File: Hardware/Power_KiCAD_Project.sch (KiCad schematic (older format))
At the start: 6 parts, among them J1 Barrel_Jack_MountingPin, J2 XT60 Cell 5, J3 XT60 Cell 4, J4 XT60 Cell 3, J5 XT60 Cell 2, J6 XT60 Cell 1

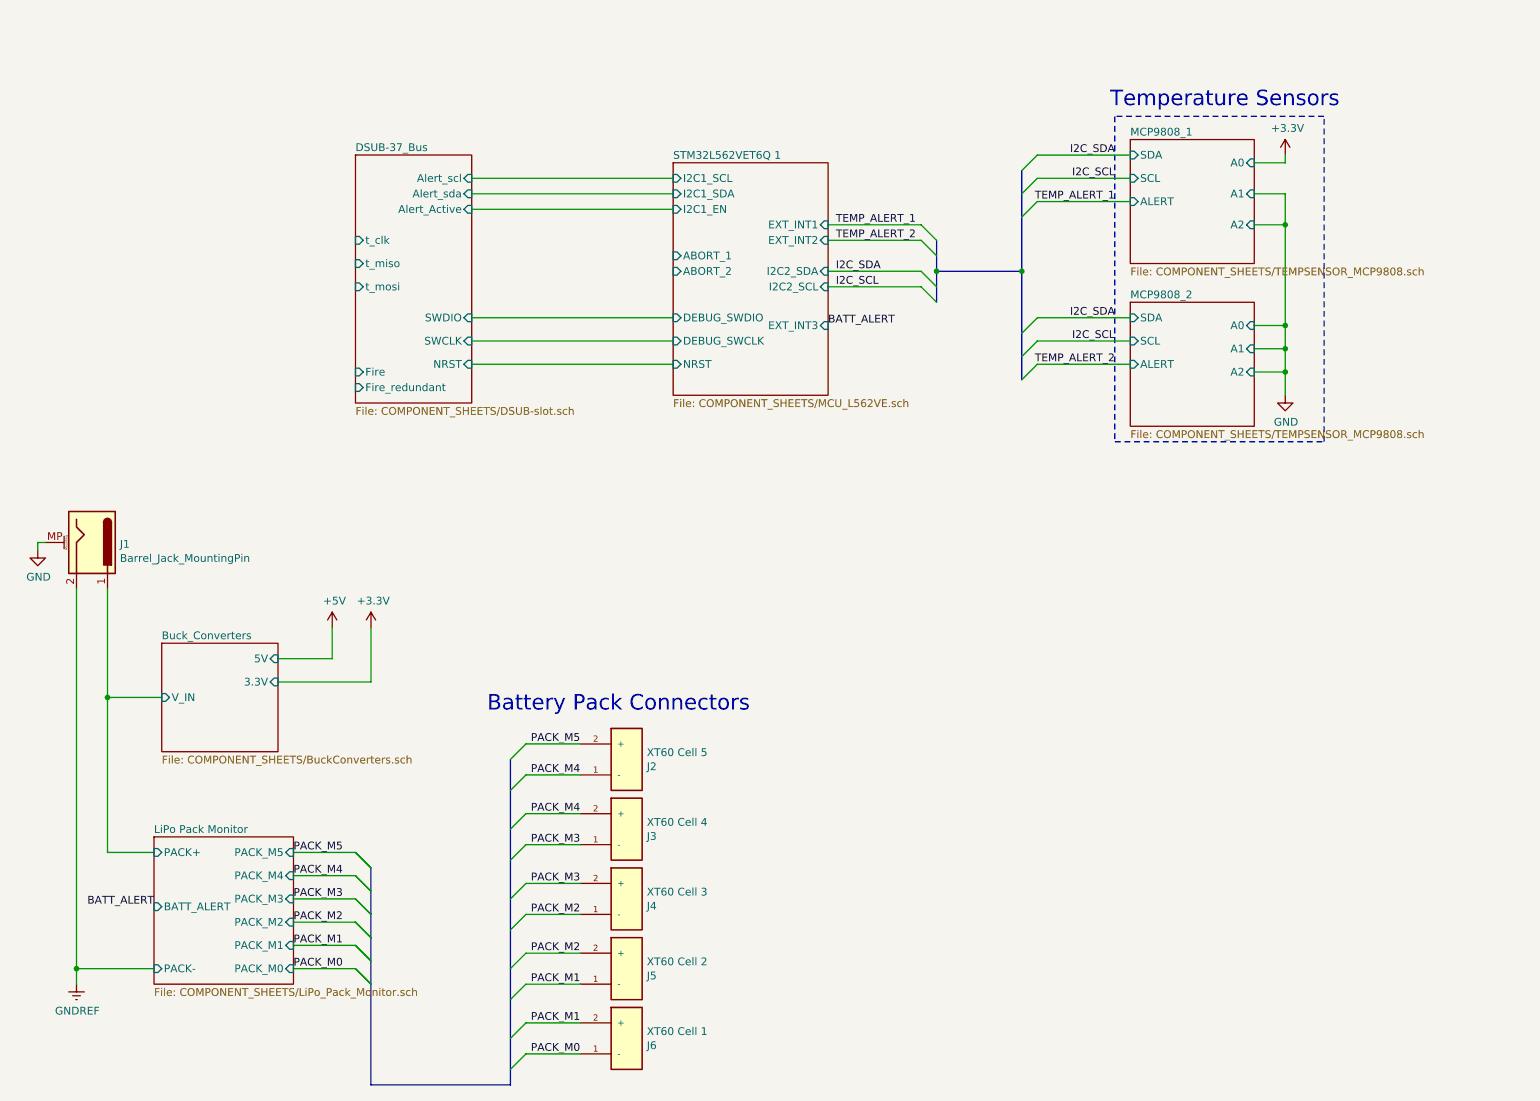
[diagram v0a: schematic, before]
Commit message: Added I2C lines to lipo monitor schematic page
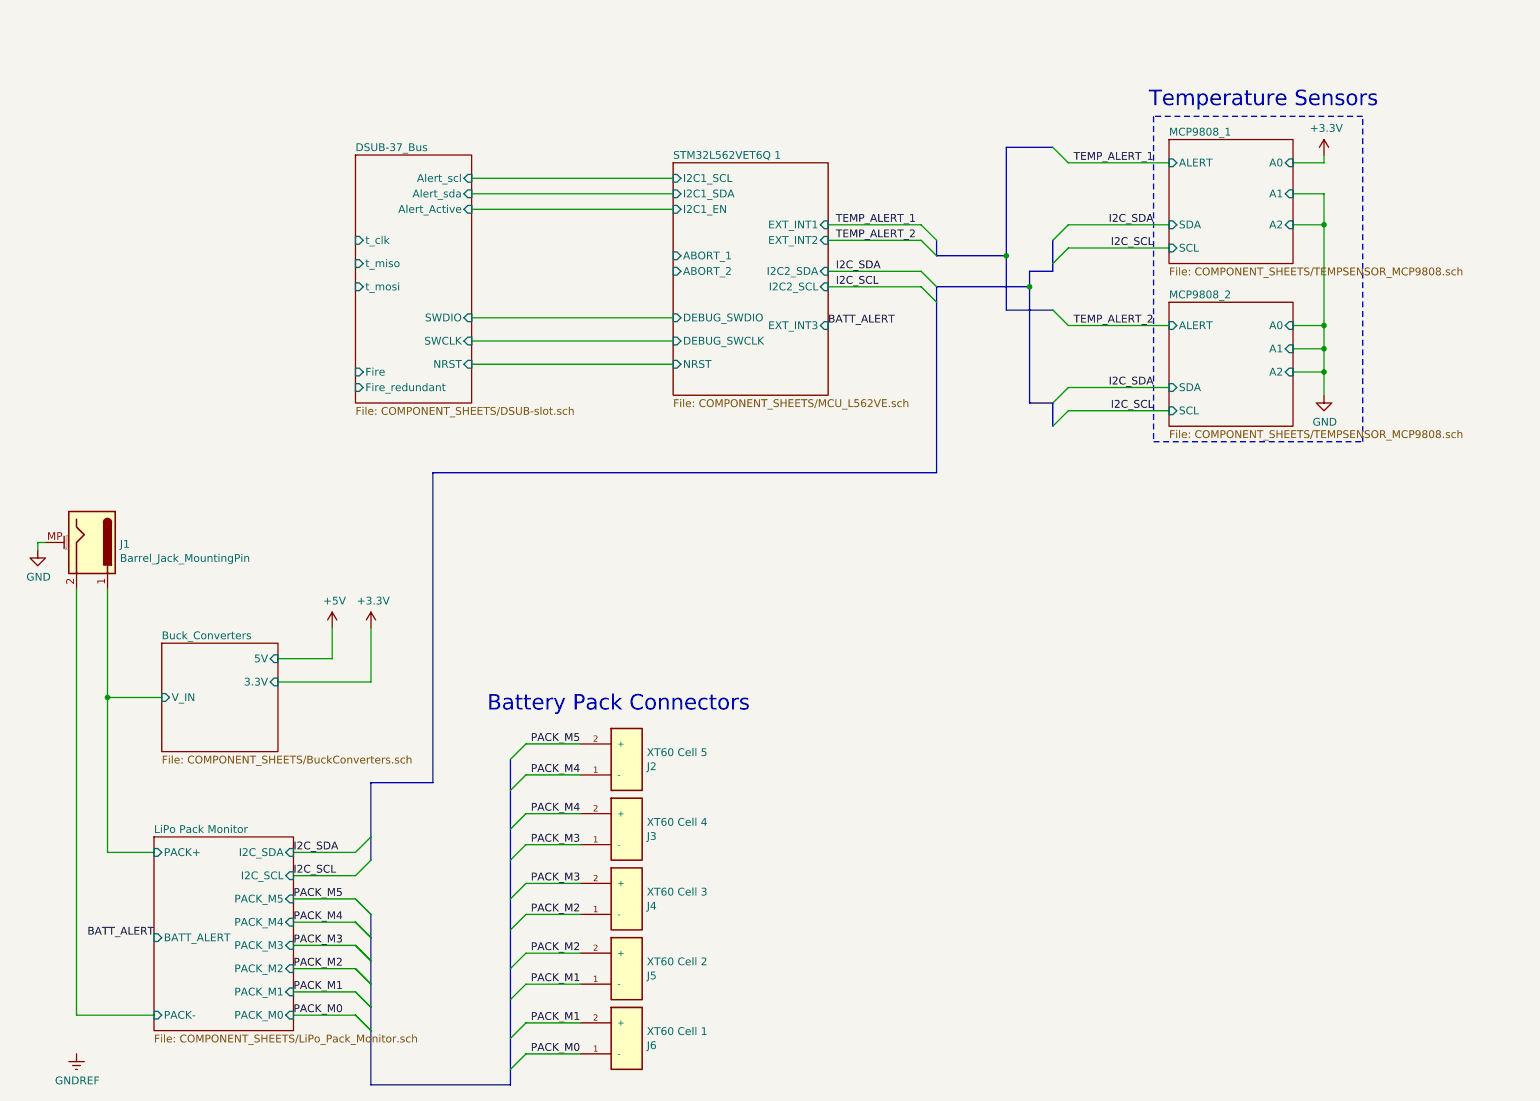
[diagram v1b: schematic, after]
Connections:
- net GNDREF: no longer J1.2
- new net LiPo Pack Monitor/PACK-: J1.2
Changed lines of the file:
@@
 L power:+3.3V #PWR05
 U 1 1 61B3C742
-P 9000 1500
-F 0 "#PWR05" H 9000 1350 50  0001 C CNN
-F 1 "+3.3V" H 9015 1673 50  0000 C CNN
-F 2 "" H 9000 1500 50  0001 C CNN
-F 3 "" H 9000 1500 50  0001 C CNN
-	1    9000 1500
+P 9250 1500
+F 0 "#PWR05" H 9250 1350 50  0001 C CNN
+F 1 "+3.3V" H 9265 1673 50  0000 C CNN
+F 2 "" H 9250 1500 50  0001 C CNN
+F 3 "" H 9250 1500 50  0001 C CNN
+	1    9250 1500
 	1    0    0    -1
 $EndComp
-Text Notes 9350 1200 2    100  ~ 0
+Text Notes 9600 1200 2    100  ~ 0
 Temperature Sensors
 $Sheet
-S 8000 2450 800  800
+S 8250 2450 800  800
 U 61B35621
 F0 "MCP9808_2" 50
 F1 "COMPONENT_SHEETS/TEMPSENSOR_MCP9808.sch" 50
-F2 "SDA" I L 8000 2550 50
-F3 "SCL" I L 8000 2700 50
-F4 "A0" I R 8800 2600 50
-F5 "A1" I R 8800 2750 50
-F6 "A2" I R 8800 2900 50
-F7 "ALERT" I L 8000 2850 50
+F2 "SDA" I L 8250 3000 50
+F3 "SCL" I L 8250 3150 50
+F4 "A0" I R 9050 2600 50
+F5 "A1" I R 9050 2750 50
+F6 "A2" I R 9050 2900 50
+F7 "ALERT" I L 8250 2600 50
 $EndSheet
 Entry Wire Line
@@
 I2C_SCL
 Wire Wire Line
-	9000 2900 8800 2900
-Wire Wire Line
-	9000 2900 9000 2750
-Wire Wire Line
-	9000 2750 8800 2750
-Wire Wire Line
-	9000 2750 9000 2600
-Wire Wire Line
-	9000 2600 8800 2600
-Connection ~ 9000 2750
-Wire Wire Line
-	8800 1950 9000 1950
-Connection ~ 9000 2600
-Wire Wire Line
-	8800 1750 9000 1750
-Wire Wire Line
-	9000 1750 9000 1950
-Connection ~ 9000 1950
-Wire Wire Line
-	8800 1550 9000 1550
-Wire Wire Line
-	9000 1550 9000 1500
+	9250 2900 9050 2900
+Wire Wire Line
+	9250 2900 9250 2750
+Wire Wire Line
+	9250 2750 9050 2750
+Wire Wire Line
+	9250 2750 9250 2600
+Wire Wire Line
+	9250 2600 9050 2600
+Connection ~ 9250 2750
+Wire Wire Line
+	9050 1950 9250 1950
+Connection ~ 9250 2600
+Wire Wire Line
+	9050 1750 9250 1750
+Wire Wire Line
+	9250 1750 9250 1950
+Connection ~ 9250 1950
+Wire Wire Line
+	9050 1550 9250 1550
+Wire Wire Line
+	9250 1550 9250 1500
 Wire Notes Line
-	9250 1250 7900 1250
+	9500 1250 8150 1250
 Entry Wire Line
 	6750 2050 6650 1950
@@
 Text Label 6100 2050 0    50   ~ 0
 TEMP_ALERT_2
-Text Label 7900 1800 2    50   ~ 0
+Text Label 8150 1550 2    50   ~ 0
 TEMP_ALERT_1
-Text Label 7900 1500 2    50   ~ 0
+Text Label 8150 1950 2    50   ~ 0
 I2C_SDA
-Text Label 7900 1650 2    50   ~ 0
+Text Label 8150 2100 2    50   ~ 0
 I2C_SCL
-Text Label 7900 2700 2    50   ~ 0
+Text Label 8150 3150 2    50   ~ 0
 I2C_SCL
-Text Label 7900 2550 2    50   ~ 0
+Text Label 8150 3000 2    50   ~ 0
 I2C_SDA
-Text Label 7900 2850 2    50   ~ 0
+Text Label 8150 2600 2    50   ~ 0
 TEMP_ALERT_2
 Entry Wire Line
-	3100 6100 3000 6000
-Entry Wire Line
-	3100 6250 3000 6150
-Entry Wire Line
 	3100 6400 3000 6300
 Entry Wire Line
@@
 	3100 6850 3000 6750
 Entry Wire Line
-	3100 6100 3000 6000
+	3100 7000 3000 6900
+Entry Wire Line
+	3100 7150 3000 7050
+Entry Wire Line
+	3100 6400 3000 6300
+Entry Wire Line
+	3100 7150 3000 7050
+Wire Wire Line
+	3000 7050 2600 7050
+Wire Wire Line
+	3000 6900 2600 6900
+Wire Wire Line
+	3000 6750 2600 6750
+Wire Wire Line
+	2600 6600 3000 6600
+Wire Wire Line
+	3000 6450 2600 6450
+Wire Wire Line
+	2600 6300 3000 6300
+Text Label 2600 6300 0    50   ~ 0
+PACK_M5
+Text Label 2600 6450 0    50   ~ 0
+PACK_M4
+Text Label 2600 6600 0    50   ~ 0
+PACK_M3
+Text Label 2600 6750 0    50   ~ 0
+PACK_M2
+Text Label 2600 6900 0    50   ~ 0
+PACK_M1
+Text Label 2600 7050 0    50   ~ 0
+PACK_M0
+Entry Wire Line
+	3100 7000 3000 6900
 Entry Wire Line
 	3100 6850 3000 6750
-Wire Wire Line
-	3000 6750 2600 6750
-Wire Wire Line
-	3000 6600 2600 6600
-Wire Wire Line
-	3000 6450 2600 6450
-Wire Wire Line
-	2600 6300 3000 6300
-Wire Wire Line
-	3000 6150 2600 6150
-Wire Wire Line
-	2600 6000 3000 6000
-Text Label 2600 6000 0    50   ~ 0
-PACK_M5
-Text Label 2600 6150 0    50   ~ 0
-PACK_M4
-Text Label 2600 6300 0    50   ~ 0
-PACK_M3
-Text Label 2600 6450 0    50   ~ 0
-PACK_M2
-Text Label 2600 6600 0    50   ~ 0
-PACK_M1
-Text Label 2600 6750 0    50   ~ 0
-PACK_M0
 Entry Wire Line
 	3100 6700 3000 6600
 Entry Wire Line
 	3100 6550 3000 6450
-Entry Wire Line
-	3100 6400 3000 6300
-Entry Wire Line
-	3100 6250 3000 6150
-Wire Wire Line
-	7400 2550 8000 2550
-Wire Wire Line
-	8000 2700 7400 2700
-Wire Wire Line
-	7400 2850 8000 2850
-Wire Wire Line
-	7400 1800 8000 1800
-Wire Wire Line
-	7400 1650 8000 1650
-Wire Wire Line
-	7400 1500 8000 1500
-Entry Wire Line
-	7300 2650 7400 2550
-Entry Wire Line
-	7300 2800 7400 2700
-Entry Wire Line
-	7300 2950 7400 2850
-Entry Wire Line
-	7300 1900 7400 1800
-Entry Wire Line
-	7300 1750 7400 1650
-Entry Wire Line
-	7300 1600 7400 1500
 Connection ~ 1400 5000
 Wire Wire Line
@@
 $EndComp
 $Sheet
-S 8000 1400 800  800
+S 8250 1400 800  800
 U 61B1B3BC
 F0 "MCP9808_1" 50
 F1 "COMPONENT_SHEETS/TEMPSENSOR_MCP9808.sch" 50
-F2 "SDA" I L 8000 1500 50
-F3 "SCL" I L 8000 1650 50
-F4 "A0" I R 8800 1550 50
-F5 "A1" I R 8800 1750 50
-F6 "A2" I R 8800 1950 50
-F7 "ALERT" I L 8000 1800 50
+F2 "SDA" I L 8250 1950 50
+F3 "SCL" I L 8250 2100 50
+F4 "A0" I R 9050 1550 50
+F5 "A1" I R 9050 1750 50
+F6 "A2" I R 9050 1950 50
+F7 "ALERT" I L 8250 1550 50
 $EndSheet
 $Sheet
@@
 $EndSheet
 $Sheet
-S 1700 5900 900  950
+S 1700 5900 900  1250
 U 615ED460
 F0 "LiPo Pack Monitor" 50
 F1 "COMPONENT_SHEETS/LiPo_Pack_Monitor.sch" 50
 F2 "PACK+" I L 1700 6000 50
-F3 "PACK_M5" I R 2600 6000 50
-F4 "PACK_M4" I R 2600 6150 50
-F5 "PACK_M3" I R 2600 6300 50
-F6 "PACK_M2" I R 2600 6450 50
-F7 "PACK_M1" I R 2600 6600 50
-F8 "PACK_M0" I R 2600 6750 50
-F9 "PACK-" I L 1700 6750 50
-F10 "BATT_ALERT" I L 1700 6350 50
+F3 "PACK_M5" I R 2600 6300 50
+F4 "PACK_M4" I R 2600 6450 50
+F5 "PACK_M3" I R 2600 6600 50
+F6 "PACK_M2" I R 2600 6750 50
+F7 "PACK_M1" I R 2600 6900 50
+F8 "PACK_M0" I R 2600 7050 50
+F9 "PACK-" I L 1700 7050 50
+F10 "BATT_ALERT" I L 1700 6550 50
+F11 "I2C_SCL" I R 2600 6150 50
+F12 "I2C_SDA" I R 2600 6000 50
 $EndSheet
 Wire Notes Line
-	7900 1250 7900 3350
+	8150 1250 8150 3350
 Wire Notes Line
-	9250 3350 9250 1250
+	9500 3350 9500 1250
 Wire Notes Line
-	7900 3350 9250 3350
+	8150 3350 9500 3350
 Wire Wire Line
 	2500 4750 2850 4750
@@
 L power:GNDREF #PWR02
 U 1 1 61C61481
-P 1200 6850
-F 0 "#PWR02" H 1200 6600 50  0001 C CNN
-F 1 "GNDREF" H 1205 6677 50  0000 C CNN
-F 2 "" H 1200 6850 50  0001 C CNN
-F 3 "" H 1200 6850 50  0001 C CNN
-	1    1200 6850
+P 1200 7300
+F 0 "#PWR02" H 1200 7050 50  0001 C CNN
+F 1 "GNDREF" H 1205 7127 50  0000 C CNN
+F 2 "" H 1200 7300 50  0001 C CNN
+F 3 "" H 1200 7300 50  0001 C CNN
+	1    1200 7300
 	1    0    0    -1
 $EndComp
@@
 Wire Wire Line
 	4450 7300 4100 7300
-Wire Wire Line
-	1200 4300 1200 6750
-Connection ~ 1200 6750
-Wire Wire Line
-	1200 6750 1200 6850
 $Sheet
 S 5050 1550 1000 1500
@@
 Text Label 6050 2600 0    50   ~ 0
 BATT_ALERT
-Text Label 1700 6350 2    50   ~ 0
+Text Label 1700 6550 2    50   ~ 0
 BATT_ALERT
 Wire Wire Line
 	1400 6000 1700 6000
-Wire Wire Line
-	1200 6750 1700 6750
 Text Notes 3850 5100 0    100  ~ 0
 Battery Pack Connectors
-Connection ~ 9000 2900
-Wire Wire Line
-	9000 3050 9000 2900
+Connection ~ 9250 2900
+Wire Wire Line
+	9250 3050 9250 2900
 $Comp
 L power:GND #PWR06
 U 1 1 61CCB2E2
-P 9000 3050
-F 0 "#PWR06" H 9000 2800 50  0001 C CNN
-F 1 "GND" H 9005 2877 50  0000 C CNN
-F 2 "" H 9000 3050 50  0001 C CNN
-F 3 "" H 9000 3050 50  0001 C CNN
-	1    9000 3050
+P 9250 3050
+F 0 "#PWR06" H 9250 2800 50  0001 C CNN
+F 1 "GND" H 9255 2877 50  0000 C CNN
+F 2 "" H 9250 3050 50  0001 C CNN
+F 3 "" H 9250 3050 50  0001 C CNN
+	1    9250 3050
 	1    0    0    -1
 $EndComp
 Wire Wire Line
-	9000 1950 9000 2600
+	9250 1950 9250 2600
 Wire Wire Line
 	1400 5000 1750 5000
@@
 Wire Wire Line
 	5050 2850 3750 2850
-Wire Bus Line
-	6750 2250 7300 2250
-Connection ~ 7300 2250
-Connection ~ 6750 2250
 $Comp
 L power:GND #PWR?
@@
 Wire Wire Line
 	3750 1850 5050 1850
-Wire Bus Line
-	6750 2050 6750 2250
-Wire Bus Line
-	6750 2250 6750 2450
-Wire Bus Line
-	7300 2250 7300 2950
-Wire Bus Line
-	7300 1600 7300 2250
-Wire Bus Line
-	3100 6100 3100 7500
+Wire Wire Line
+	1200 7050 1700 7050
+Wire Wire Line
+	1200 4300 1200 7050
+Wire Wire Line
+	2600 6150 3000 6150
+Wire Wire Line
+	2600 6000 3000 6000
+Text Label 2600 6150 0    50   ~ 0
+I2C_SCL
+Text Label 2600 6000 0    50   ~ 0
+I2C_SDA
+Entry Wire Line
+	3000 6150 3100 6050
+Entry Wire Line
+	3000 6000 3100 5900
+Wire Bus Line
+	3100 5550 3500 5550
+Wire Bus Line
+	3500 5550 3500 3550
+Wire Bus Line
+	3500 3550 6750 3550
+Wire Bus Line
+	6750 2050 6750 2150
+Wire Bus Line
+	6750 2150 7200 2150
+Entry Wire Line
+	7600 1950 7500 2050
+Entry Wire Line
+	7600 2100 7500 2200
+Entry Wire Line
+	7600 3000 7500 3100
+Entry Wire Line
+	7600 3150 7500 3250
+Entry Wire Line
+	7600 2600 7500 2500
+Entry Wire Line
+	7600 1550 7500 1450
+Wire Bus Line
+	7500 3250 7500 3100
+Wire Bus Line
+	7500 3100 7350 3100
+Wire Bus Line
+	7200 2150 7200 1450
+Wire Bus Line
+	7200 1450 7500 1450
+Wire Bus Line
+	7500 2500 7200 2500
+Wire Bus Line
+	6750 2350 7350 2350
+Wire Bus Line
+	7200 2500 7200 2150
+Connection ~ 7200 2150
+Wire Bus Line
+	7350 2350 7350 3100
+Wire Bus Line
+	7350 2350 7350 2250
+Wire Bus Line
+	7350 2250 7500 2250
+Connection ~ 7350 2350
+Wire Wire Line
+	7600 1950 8250 1950
+Wire Wire Line
+	7600 2100 8250 2100
+Wire Wire Line
+	7600 2600 8250 2600
+Wire Wire Line
+	7600 3000 8250 3000
+Wire Wire Line
+	7600 3150 8250 3150
+Wire Wire Line
+	7600 1550 8250 1550
+Wire Bus Line
+	3100 5550 3100 6050
+Wire Bus Line
+	6750 2350 6750 3550
+Wire Bus Line
+	7500 2050 7500 2250
+Wire Bus Line
+	3100 6400 3100 7500
 Wire Bus Line
 	4000 5400 4000 7500

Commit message: Moved external switch connector to pack+, added missing no connection flags
This change renders the current PCB layout defunct, next commits will be redesigns of the layout.
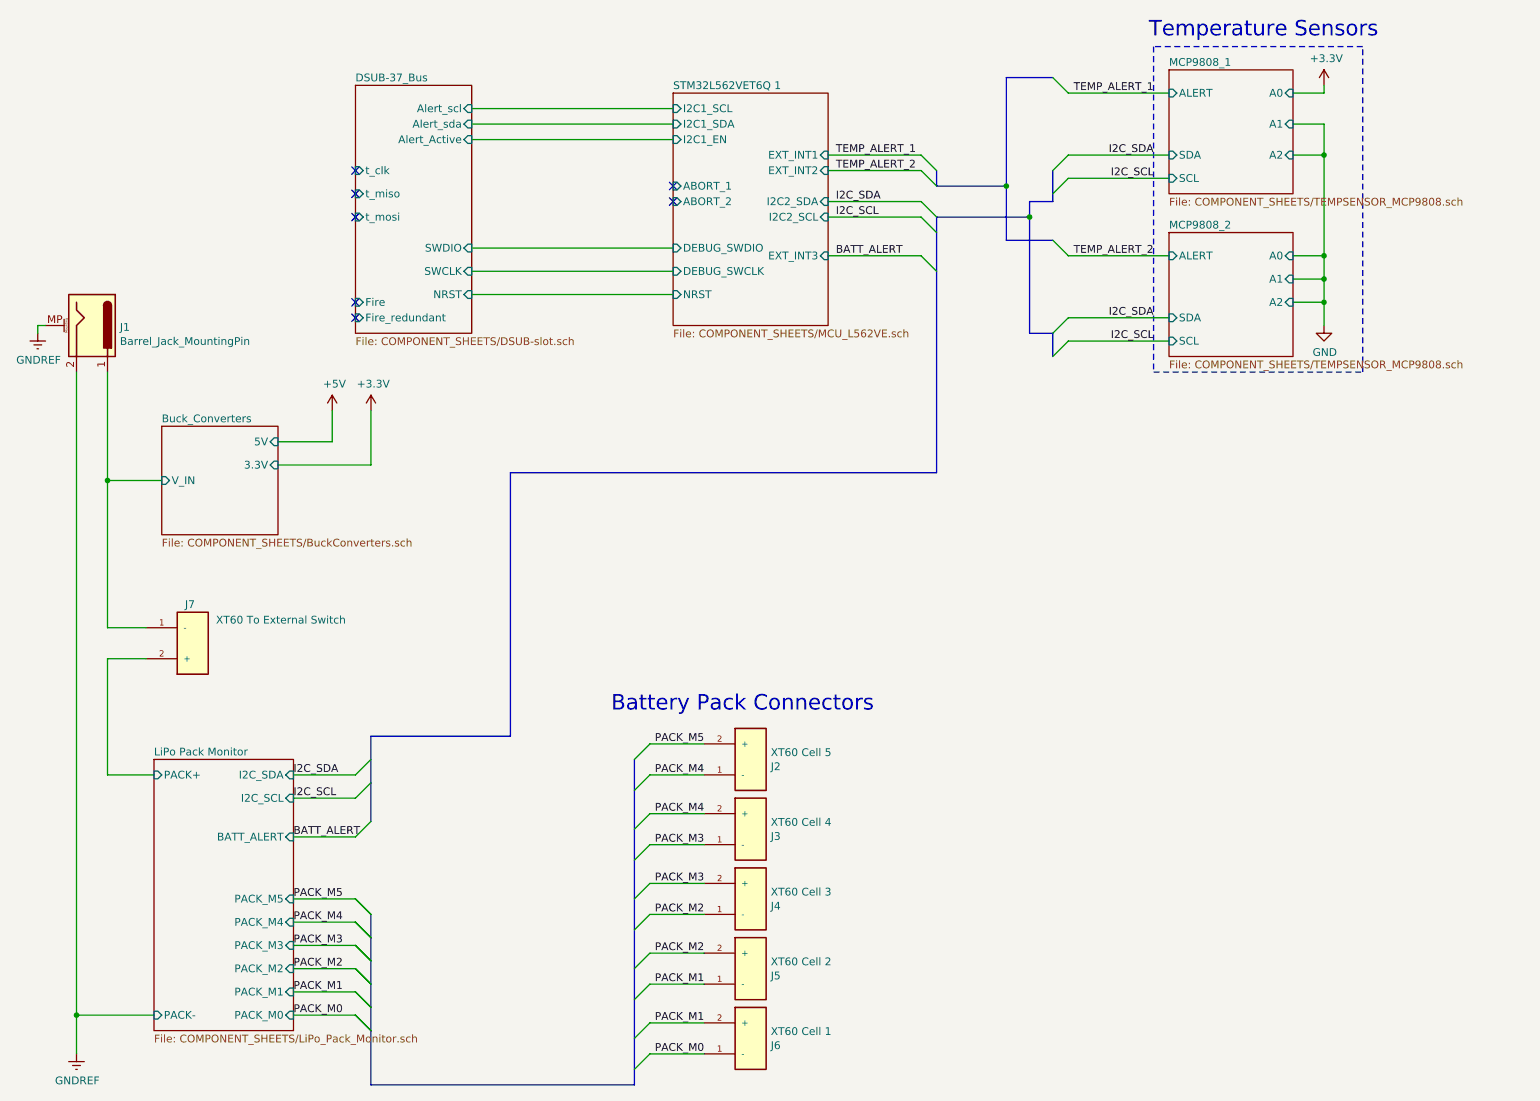
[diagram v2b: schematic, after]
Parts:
- added J7: XT60 To External Switch, RDT_Custom_Footprints:AMASS_XT60-M, symbol Power_KiCAD_Project-rescue:XT60-M-XT60-M-Power_KiCAD_Project-rescue
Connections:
- net LiPo Pack Monitor/PACK- is gone; now on net GNDREF: J1.2
- net Buck_Converters/V_IN: now also J7.1 (-)
- net GND: no longer J1.MP (MountPin)
- net GNDREF: now also J1.MP (MountPin)
- new net LiPo Pack Monitor/PACK+: J7.2 (+)
- no-connect marks 0 -> 7
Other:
- moved on the sheet: J1, J2, J3, J4, J5, J6
